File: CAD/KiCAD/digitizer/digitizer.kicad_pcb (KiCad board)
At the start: 2 copper layers, 64 parts, among them J10a Conn_02x40_Odd_Even, J10b Conn_02x24_Odd_Even, J11a Conn_02x40_Odd_Even, J11b Conn_02x24_Odd_Even, J12a Conn_02x40_Odd_Even, J12b Conn_02x24_Odd_Even, J13a Conn_02x40_Odd_Even, J13b Conn_02x24_Odd_Even, J14a Conn_02x40_Odd_Even, J14b Conn_02x24_Odd_Even, J15a Conn_02x40_Odd_Even, J15b Conn_02x24_Odd_Even, J16a Conn_02x40_Odd_Even, J16b Conn_02x24_Odd_Even, J17a Conn_02x40_Odd_Even, J17b Conn_02x24_Odd_Even, J18a Conn_02x40_Odd_Even, J18b Conn_02x24_Odd_Even, J19a Conn_02x40_Odd_Even, J19b Conn_02x24_Odd_Even, J1a Conn_02x40_Odd_Even, J1b Conn_02x24_Odd_Even, J20a Conn_02x40_Odd_Even, J20b Conn_02x24_Odd_Even, J21a Conn_02x40_Odd_Even, J21b Conn_02x24_Odd_Even, J22a Conn_02x40_Odd_Even, J22b Conn_02x24_Odd_Even, J23a Conn_02x40_Odd_Even, J23b Conn_02x24_Odd_Even, J24a Conn_02x40_Odd_Even, J24b Conn_02x24_Odd_Even, J25a Conn_02x40_Odd_Even, J25b Conn_02x24_Odd_Even, J26a Conn_02x40_Odd_Even, J26b Conn_02x24_Odd_Even, J27a Conn_02x40_Odd_Even, J27b Conn_02x24_Odd_Even, J28a Conn_02x40_Odd_Even, J28b Conn_02x24_Odd_Even, J29a Conn_02x40_Odd_Even, J29b Conn_02x24_Odd_Even, J2a Conn_02x40_Odd_Even, J2b Conn_02x24_Odd_Even, J30a Conn_02x40_Odd_Even, J30b Conn_02x24_Odd_Even, J31a Conn_02x40_Odd_Even, J31b Conn_02x24_Odd_Even, J32a Conn_02x40_Odd_Even, J32b Conn_02x24_Odd_Even, J3a Conn_02x40_Odd_Even, J3b Conn_02x24_Odd_Even, J4a Conn_02x40_Odd_Even, J4b Conn_02x24_Odd_Even, J5a Conn_02x40_Odd_Even, J5b Conn_02x24_Odd_Even, J6a Conn_02x40_Odd_Even, J6b Conn_02x24_Odd_Even, J7a Conn_02x40_Odd_Even, J7b Conn_02x24_Odd_Even, J8a Conn_02x40_Odd_Even, J8b Conn_02x24_Odd_Even, J9a Conn_02x40_Odd_Even, J9b Conn_02x24_Odd_Even

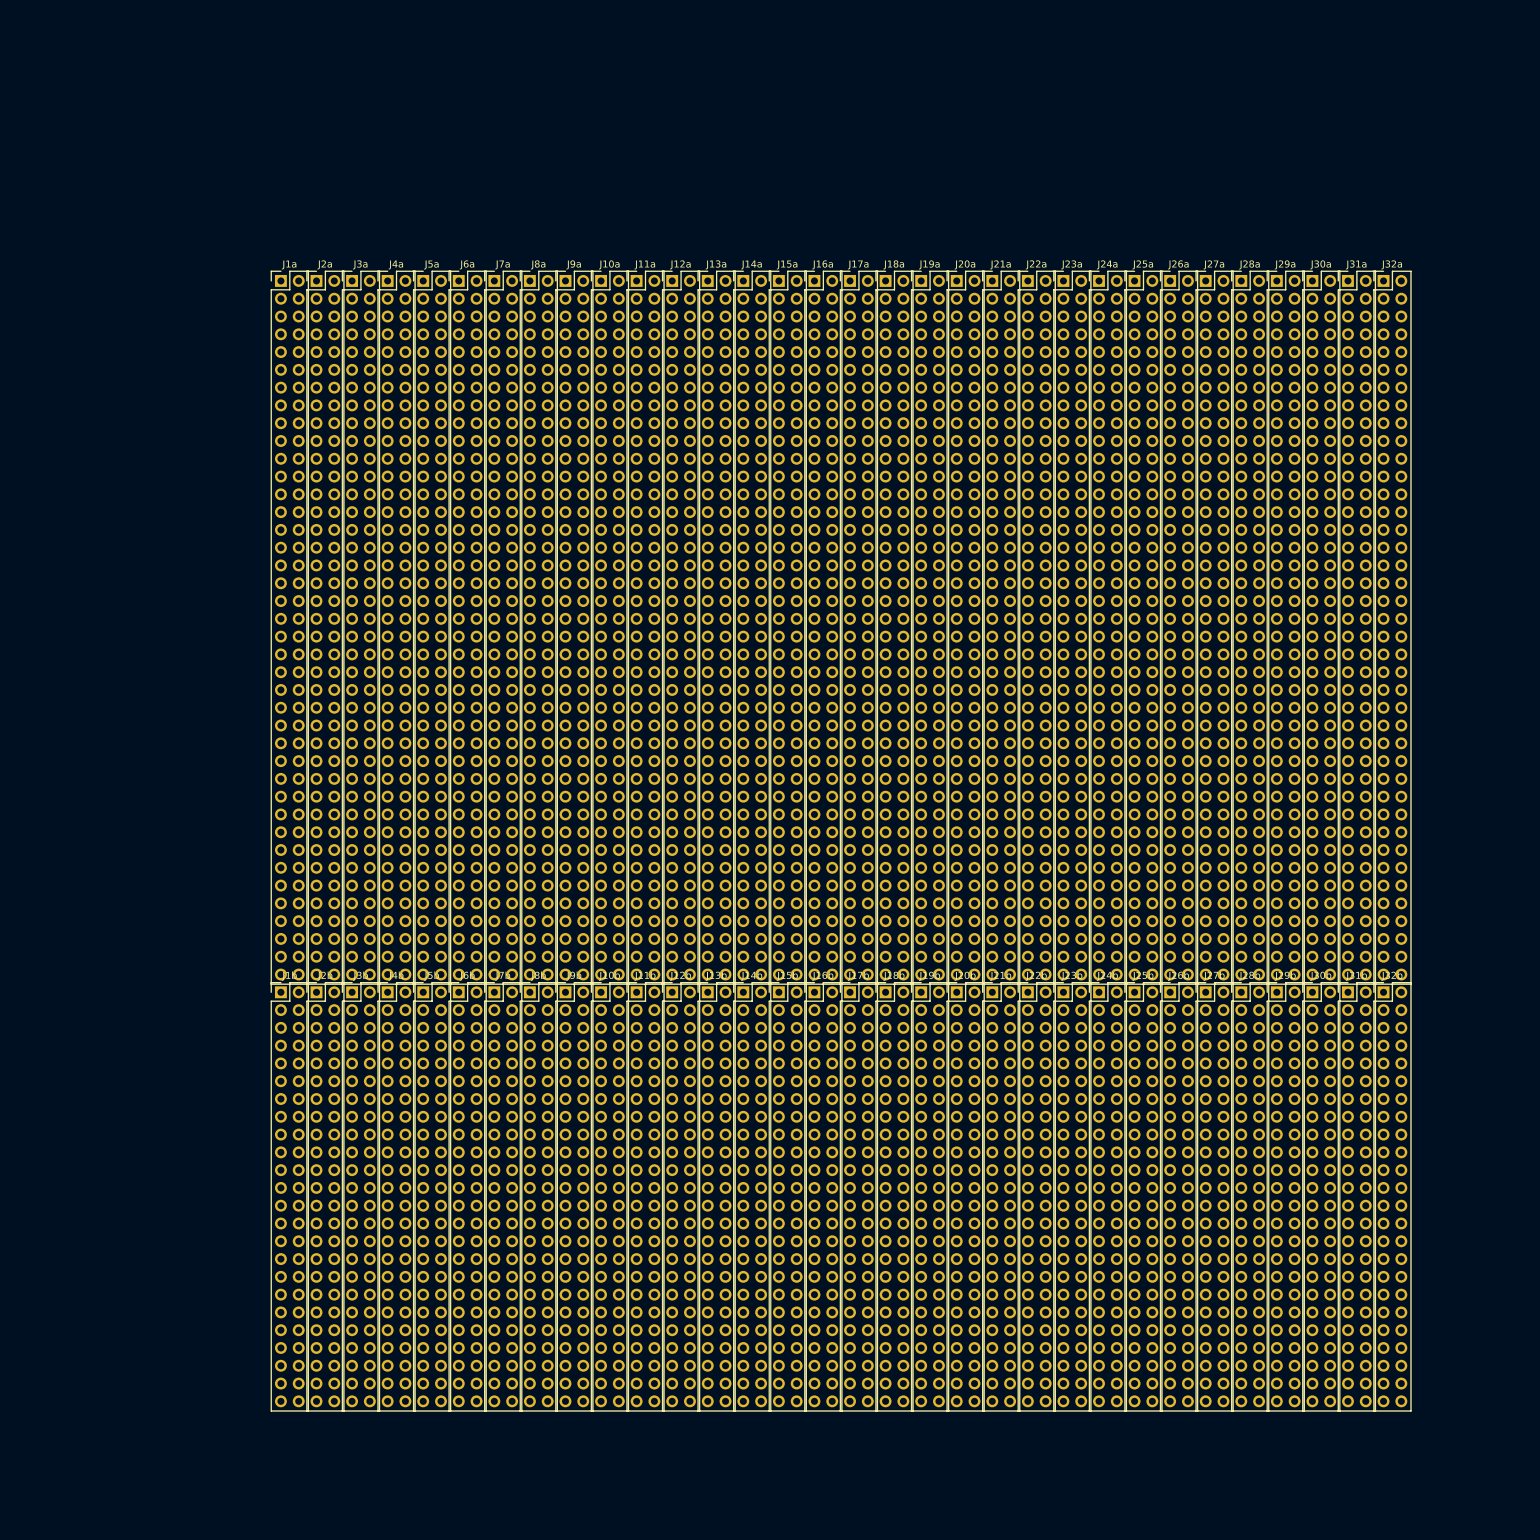
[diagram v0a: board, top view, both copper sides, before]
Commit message: add digitizer tracks
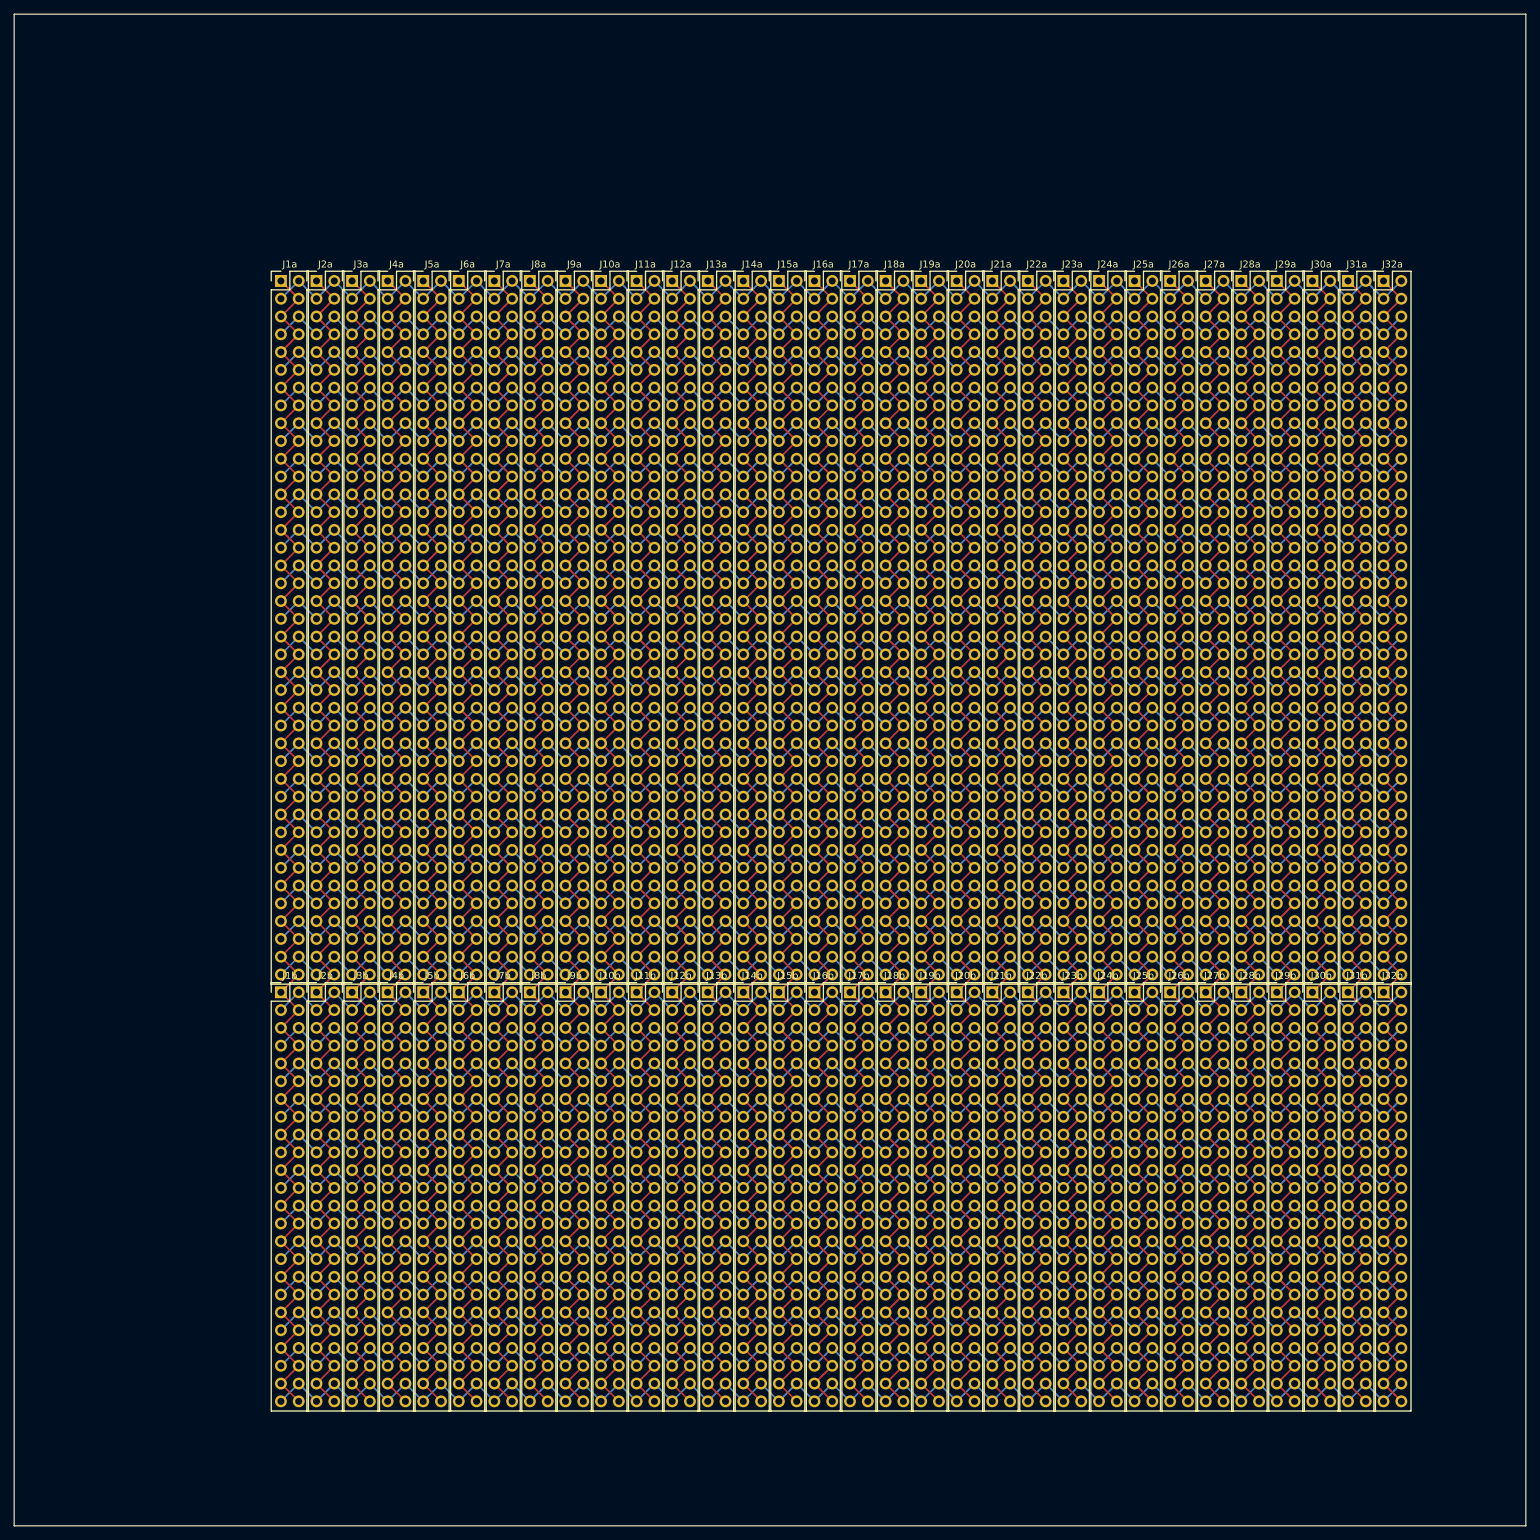
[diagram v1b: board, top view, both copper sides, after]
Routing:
- net C29: track 0.00 -> 226.3 mm
- net R18: track 0.00 -> 226.3 mm
- net C22: track 0.00 -> 226.3 mm
- net R25: track 0.00 -> 226.3 mm
- net R16: track 0.00 -> 226.3 mm
- net C32: track 0.00 -> 226.3 mm
- net C30: track 0.00 -> 226.3 mm
- net C2: track 0.00 -> 226.3 mm
- net C13: track 0.00 -> 226.3 mm
- net R20: track 0.00 -> 226.3 mm
- net C4: track 0.00 -> 226.3 mm
- net C28: track 0.00 -> 226.3 mm
- net C11: track 0.00 -> 226.3 mm
- net R27: track 0.00 -> 226.3 mm
- net C20: track 0.00 -> 226.3 mm
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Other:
- board outline added: 215.9 x 215.9 mm

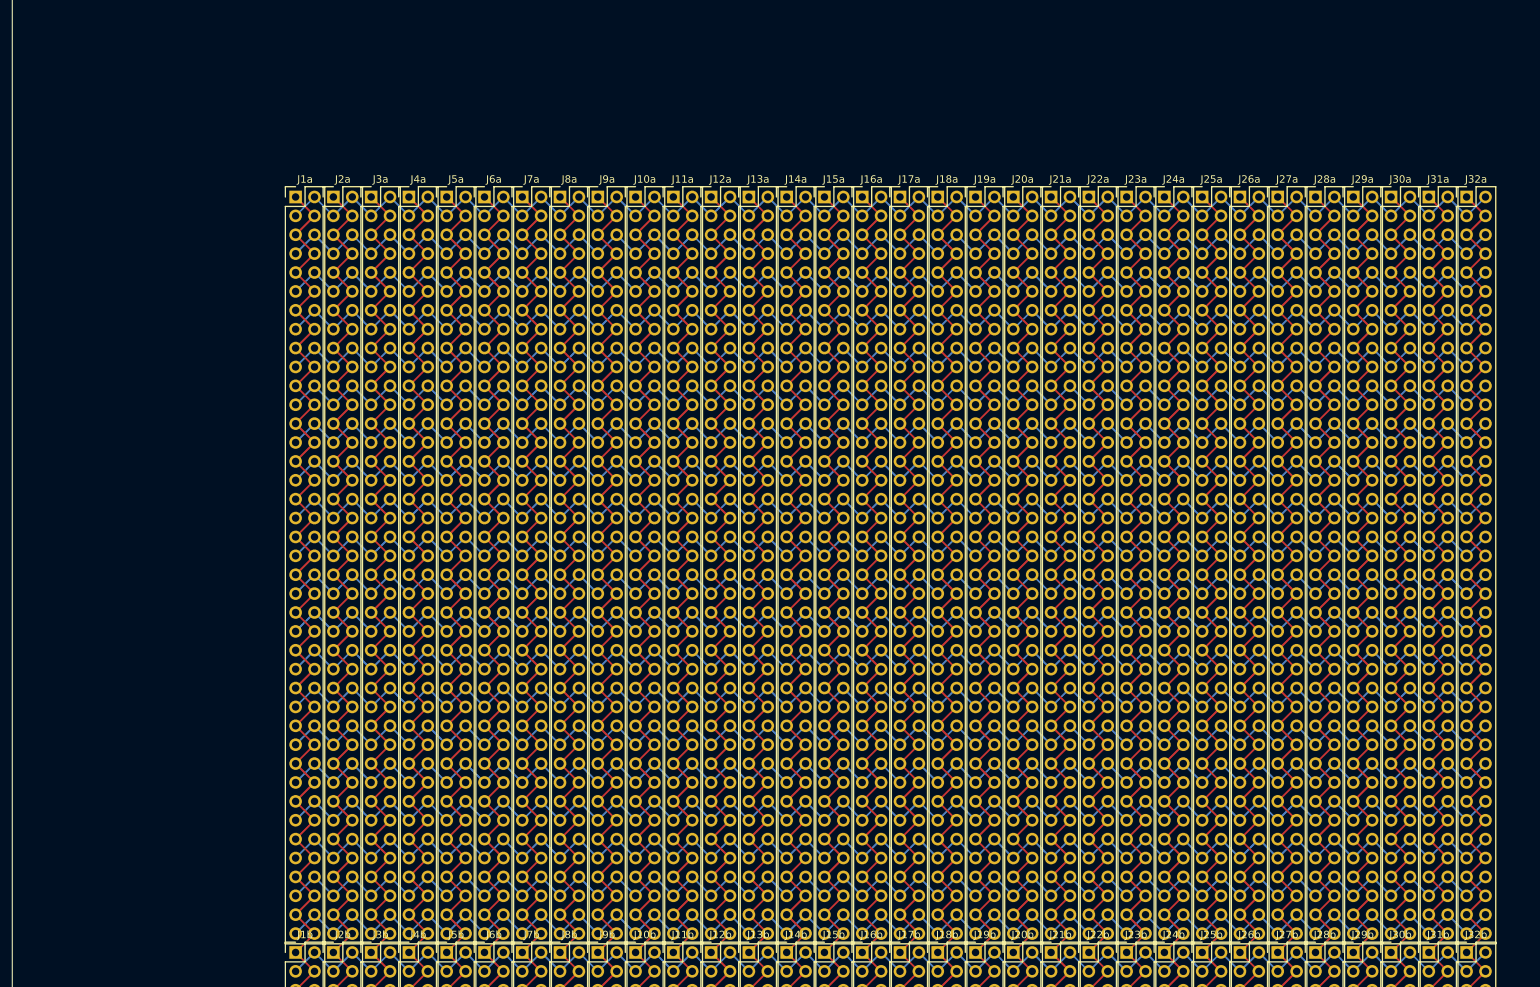
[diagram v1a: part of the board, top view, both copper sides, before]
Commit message: one MCP23017 added and routed
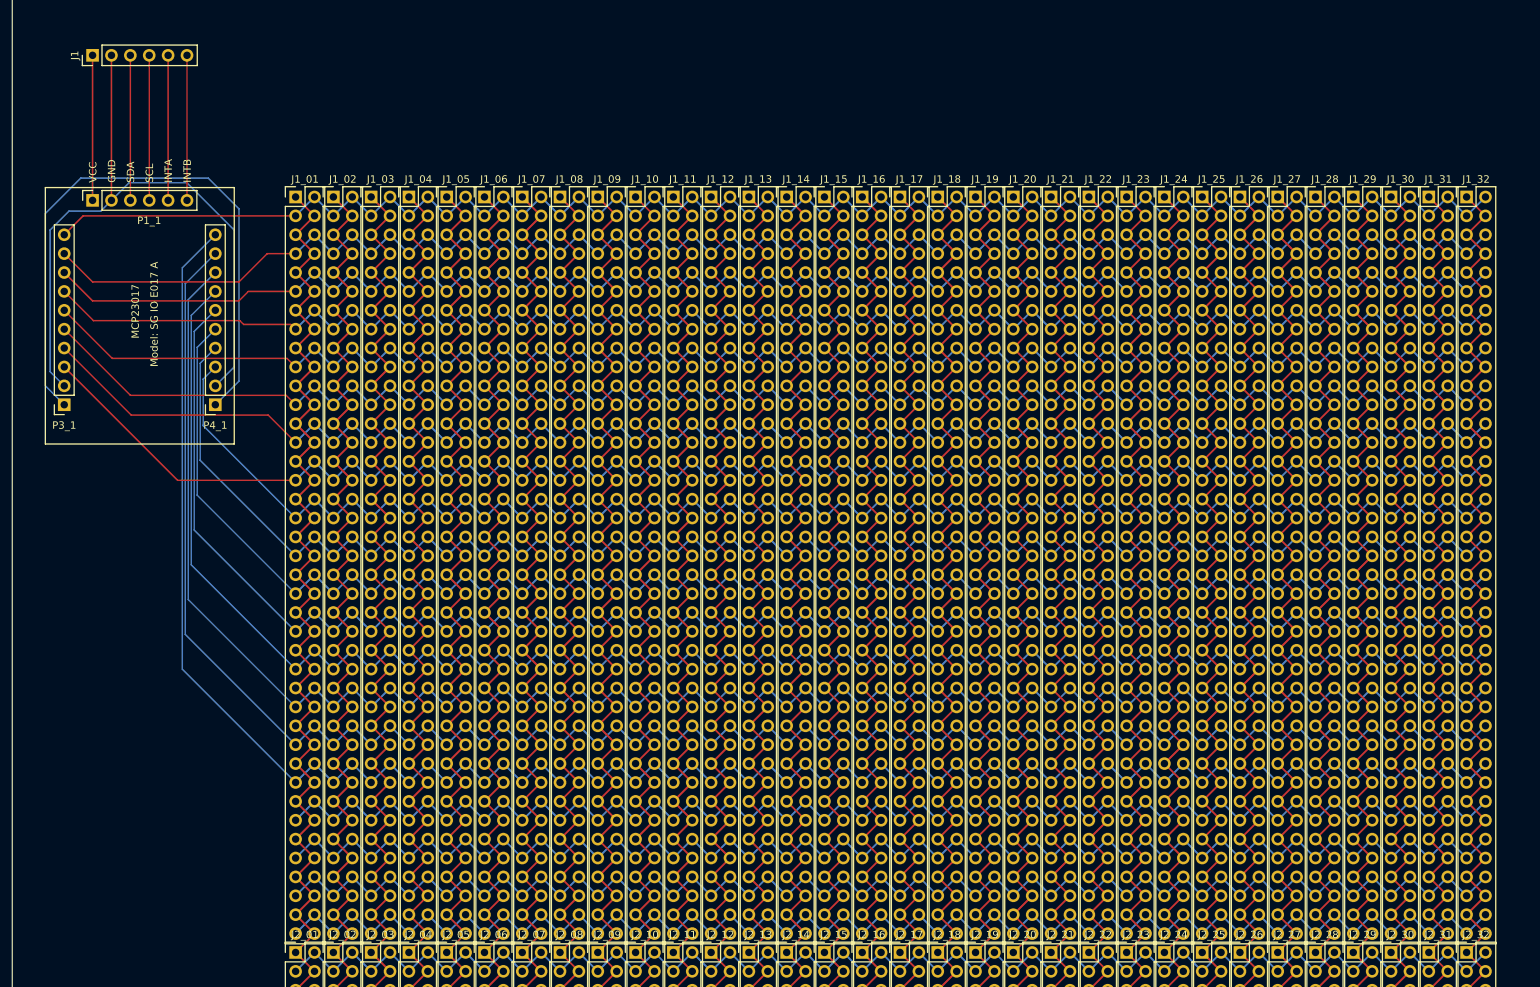
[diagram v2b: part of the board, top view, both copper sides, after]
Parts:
- added J1: Conn_01x06, Connector_PinHeader_2.54mm:PinHeader_1x06_P2.54mm_Vertical, F.Cu at (97.2, 52.8)
- added P1_1: Conn_01x06, Connector_PinSocket_2.54mm:PinSocket_1x06_P2.54mm_Vertical, F.Cu at (97.2, 72.3)
- added P3_1: Conn_01x10, Connector_PinSocket_2.54mm:PinSocket_1x10_P2.54mm_Vertical, F.Cu at (93.3, 99.8)
- added P4_1: Conn_01x10, Connector_PinSocket_2.54mm:PinSocket_1x10_P2.54mm_Vertical, F.Cu at (113.7, 99.8)
- renumbered J1a to J1_01, J2a to J1_02, J3a to J1_03, J4a to J1_04, J5a to J1_05, J6a to J1_06, J7a to J1_07, J8a to J1_08, J9a to J1_09, J10a to J1_10, J11a to J1_11, J12a to J1_12, J13a to J1_13, J14a to J1_14, J15a to J1_15, J16a to J1_16, J17a to J1_17, J18a to J1_18, J19a to J1_19, J20a to J1_20, J21a to J1_21, J22a to J1_22, J23a to J1_23, J24a to J1_24, J25a to J1_25, J26a to J1_26, J27a to J1_27, J28a to J1_28, J29a to J1_29, J30a to J1_30, J31a to J1_31, J32a to J1_32, J1b to J2_01, J2b to J2_02, J3b to J2_03, J4b to J2_04, J5b to J2_05, J6b to J2_06, J7b to J2_07, J8b to J2_08, J9b to J2_09, J10b to J2_10, J11b to J2_11, J12b to J2_12, J13b to J2_13, J14b to J2_14, J15b to J2_15, J16b to J2_16, J17b to J2_17, J18b to J2_18, J19b to J2_19, J20b to J2_20, J21b to J2_21, J22b to J2_22, J23b to J2_23, J24b to J2_24, J25b to J2_25, J26b to J2_26, J27b to J2_27, J28b to J2_28, J29b to J2_29, J30b to J2_30, J31b to J2_31, J32b to J2_32
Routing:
- net VCC: track 0.00 -> 106.9 mm
- net GND: track 0.00 -> 93.3 mm
- net R16: track 226.3 -> 308.1 mm
- net R15: track 226.3 -> 300.2 mm
- net R14: track 226.3 -> 292.2 mm
- net R13: track 226.3 -> 284.3 mm
- net R12: track 226.3 -> 276.3 mm
- net R11: track 226.3 -> 268.4 mm
- net R8: track 226.3 -> 263.7 mm
- net R7: track 226.3 -> 262.7 mm
- net R6: track 226.3 -> 261.6 mm
- net R5: track 226.3 -> 260.6 mm
- net R2: track 226.3 -> 260.6 mm
- net R10: track 226.3 -> 260.4 mm
- net R4: track 226.3 -> 259.5 mm
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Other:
- board text added: "GND"
- board text added: "INTA"
- board text added: "INTB"
- board text added: "MCP23017"
- board text added: "Model: SG IO E017 A"
- board text added: "SCL"
- board text added: "SDA"
- board text added: "VCC"

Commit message: routing wip take 1
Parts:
- moved J1 262.3 mm to (354.5, 103.5), turned to 0 degrees
- moved P1_1 231.6 mm to (326.7, 103.6), turned to 0 degrees
- moved P3_1 205.8 mm to (299.2, 99.8), turned to 90 degrees
- moved P4_1 186.6 mm to (299.2, 120.1), turned to 90 degrees
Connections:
- P3_1 pad 1: VCC -> unconnected-(P3_1-Pin_1-Pad1)
- P3_1 pad 2: GND -> unconnected-(P3_1-Pin_2-Pad2)
- P4_1 pad 1: VCC -> unconnected-(P4_1-Pin_1-Pad1)
- P4_1 pad 2: GND -> unconnected-(P4_1-Pin_2-Pad2)
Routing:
- net VCC: track 106.9 -> 0.00 mm
- net GND: track 93.3 -> 0.00 mm
- net R16: track 308.1 -> 275.4 mm
- net R15: track 300.2 -> 270.8 mm
- net R14: track 292.2 -> 266.2 mm
- net R13: track 284.3 -> 261.5 mm
- net SDA: track 19.5 -> 0.00 mm
- net SCL: track 19.5 -> 0.00 mm
- net INTB: track 19.5 -> 0.00 mm
- net INTA: track 19.5 -> 0.00 mm
- net R12: track 276.3 -> 256.9 mm
- net R1: track 258.5 -> 275.4 mm
- net R8: track 263.7 -> 249.2 mm
- net R11: track 268.4 -> 254.3 mm
- net R7: track 262.7 -> 251.8 mm
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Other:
- board size 215.9 x 215.9 mm -> 345.4 x 209.6 mm

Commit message: digitizer draft with MCP23017 routing
Made-with: Cursor
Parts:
- added P1_2: Conn_01x06, Connector_PinSocket_2.54mm:PinSocket_1x06_P2.54mm_Vertical, F.Cu at (261.2, 212.9)
- added P1_3: Conn_01x06, Connector_PinSocket_2.54mm:PinSocket_1x06_P2.54mm_Vertical, F.Cu at (80.0, 44.4)
- added P1_4: Conn_01x06, Connector_PinSocket_2.54mm:PinSocket_1x06_P2.54mm_Vertical, F.Cu at (163.8, 44.3)
- added P3_2: Conn_01x10, Connector_PinSocket_2.54mm:PinSocket_1x10_P2.54mm_Vertical, F.Cu at (233.7, 209.0)
- added P3_3: Conn_01x10, Connector_PinSocket_2.54mm:PinSocket_1x10_P2.54mm_Vertical, F.Cu at (76.2, 71.9)
- added P3_4: Conn_01x10, Connector_PinSocket_2.54mm:PinSocket_1x10_P2.54mm_Vertical, F.Cu at (160.0, 71.8)
- added P4_2: Conn_01x10, Connector_PinSocket_2.54mm:PinSocket_1x10_P2.54mm_Vertical, F.Cu at (233.7, 229.4)
- added P4_3: Conn_01x10, Connector_PinSocket_2.54mm:PinSocket_1x10_P2.54mm_Vertical, F.Cu at (96.5, 71.9)
- added P4_4: Conn_01x10, Connector_PinSocket_2.54mm:PinSocket_1x10_P2.54mm_Vertical, F.Cu at (180.3, 71.8)
- moved J1 185.1 mm to (251.5, 257.3), turned to -90 degrees
- moved J2_06 80.3 mm to (73.7, 198.9)
- moved J2_08 80.3 mm to (83.8, 198.9)
- moved J2_15 80.3 mm to (119.4, 198.9)
- moved J2_17 80.3 mm to (129.5, 198.9)
- moved J2_19 80.3 mm to (139.7, 198.9)
- moved J2_24 80.3 mm to (165.1, 198.9)
- moved J2_26 80.3 mm to (175.3, 198.9)
- moved J2_27 80.3 mm to (180.3, 198.9)
- moved J2_28 80.3 mm to (185.4, 198.9)
- moved J2_31 80.3 mm to (200.7, 198.9)
- moved J1_06 80.3 mm to (73.7, 97.3)
- moved J1_08 80.3 mm to (83.8, 97.3)
- moved J1_15 80.3 mm to (119.4, 97.3)
- moved J1_17 80.3 mm to (129.5, 97.3)
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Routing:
- net INTB: track 0.00 -> 463.0 mm, vias 0 -> 4
- net INTA: track 0.00 -> 462.8 mm, vias 0 -> 4
- net SCL: track 0.00 -> 462.6 mm, vias 0 -> 4
- net SDA: track 0.00 -> 462.3 mm, vias 0 -> 4
- net GND: track 0.00 -> 462.2 mm, vias 0 -> 4
- net VCC: track 0.00 -> 462.0 mm, vias 0 -> 4
- net C17: track 226.3 -> 287.2 mm
- net R17: track 226.3 -> 287.2 mm
- net C16: track 226.3 -> 286.1 mm
- net C1: track 226.3 -> 286.1 mm
- net C32: track 226.3 -> 285.1 mm
- net R32: track 226.3 -> 285.1 mm
- net C18: track 226.3 -> 282.6 mm
- net R18: track 226.3 -> 282.5 mm
- net C15: track 226.3 -> 281.5 mm
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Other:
- board size 345.4 x 209.6 mm -> 254 x 254 mm
- board text added: "@servernoj 03/26"
- board text added: "C1"
- board text added: "C32"
- board text added: "Cheroma digitizer"
- board text added: "R1"
- board text added: "R32"
- board text added: "v1.0"
